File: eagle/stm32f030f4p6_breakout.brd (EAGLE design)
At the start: 25.4 x 15.2 mm, 10 parts, among them U1 STM32F030F4PXTSSOP20

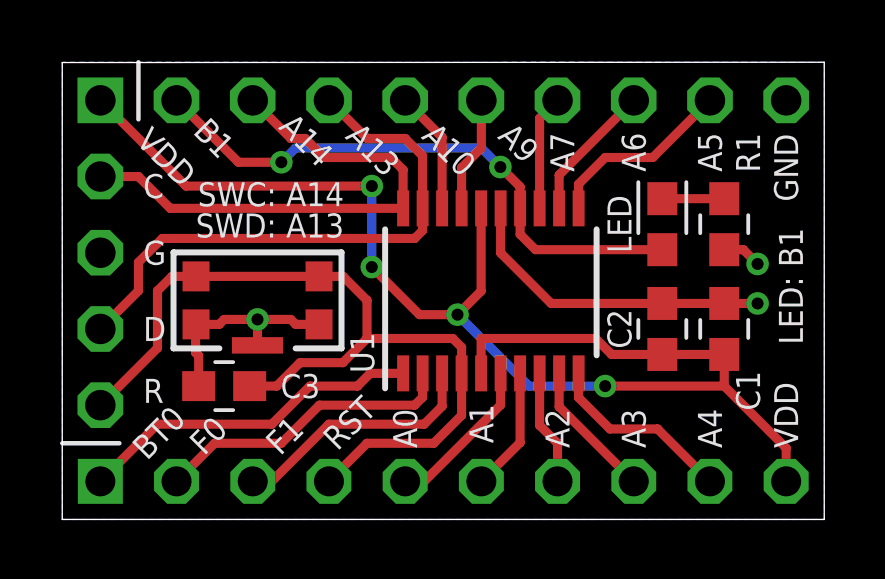
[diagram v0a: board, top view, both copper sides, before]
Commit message: - added BOOT0 pulldown - silkscreen type slightly increased to 35mil - wider supply tracks - minor changes to routing
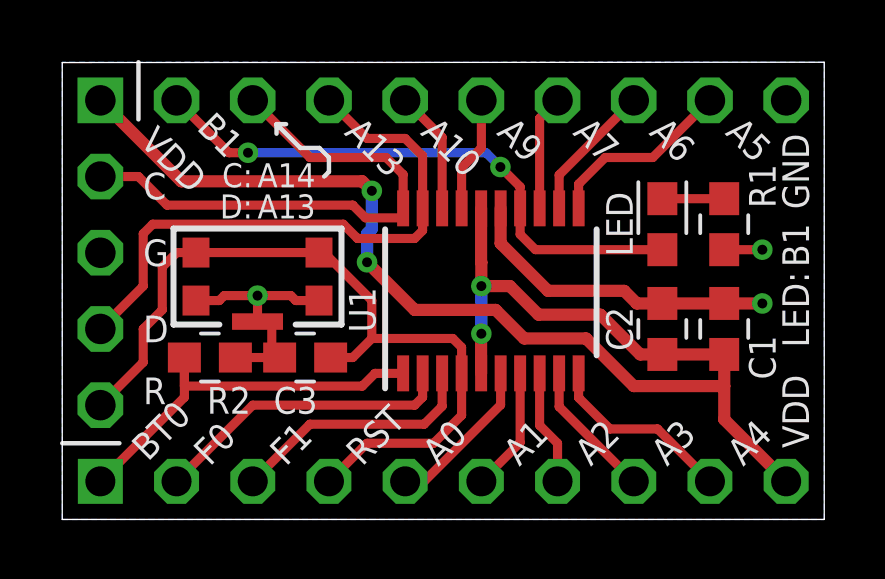
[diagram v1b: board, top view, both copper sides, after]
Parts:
- added R2: 10k, rcl_smd:R0603
- moved C3 2.86 mm to (8.10, 5.40)
- moved RESET 0.79 mm to (6.51, 8.10)
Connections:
- net BOOT0: now also R2.2
- net GND: now also R2.1
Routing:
- net BOOT0: track 11.6 -> 13.7 mm
- net NRST: track 28.8 -> 26.9 mm
- net GND: track 19.3 -> 20.5 mm
- net VDD: track 44.8 -> 46.0 mm
- net PA13: track 19.0 -> 19.9 mm
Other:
- board text added: "C: D:"
- board text added: "U1: STM32F030F4P6 C1: 100n C2: 10n C3: 100n R1: 330 Ohm R2: 10k"
- board text removed: "A14"
- board text removed: "SWC: SWD:"
- board text removed: "U1: STM32F030F4P6 C1: 100n C2: 10n C3: 100n R1: 330 Ohm"
